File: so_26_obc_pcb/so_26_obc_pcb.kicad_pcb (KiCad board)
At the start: 4 copper layers, 90.2 x 95.9 mm, 52 parts, among them J1 Conn_02x12_Odd_Even, J10 Conn_01x02, J2 Conn_02x06_Odd_Even, J3 Conn_01x04, J4 Conn_01x03, J5 Conn_01x02, J7 Conn_01x03, J8 Conn_01x03, J9 Conn_01x02, SW1 SW_Push, U1 STM32G431RBTx, U2 TPT3232A-TS3R, U3 PCT2075, U4 MPRLS0025, U5 LSM6DS3, U6 MEM2067-02-180-00-A

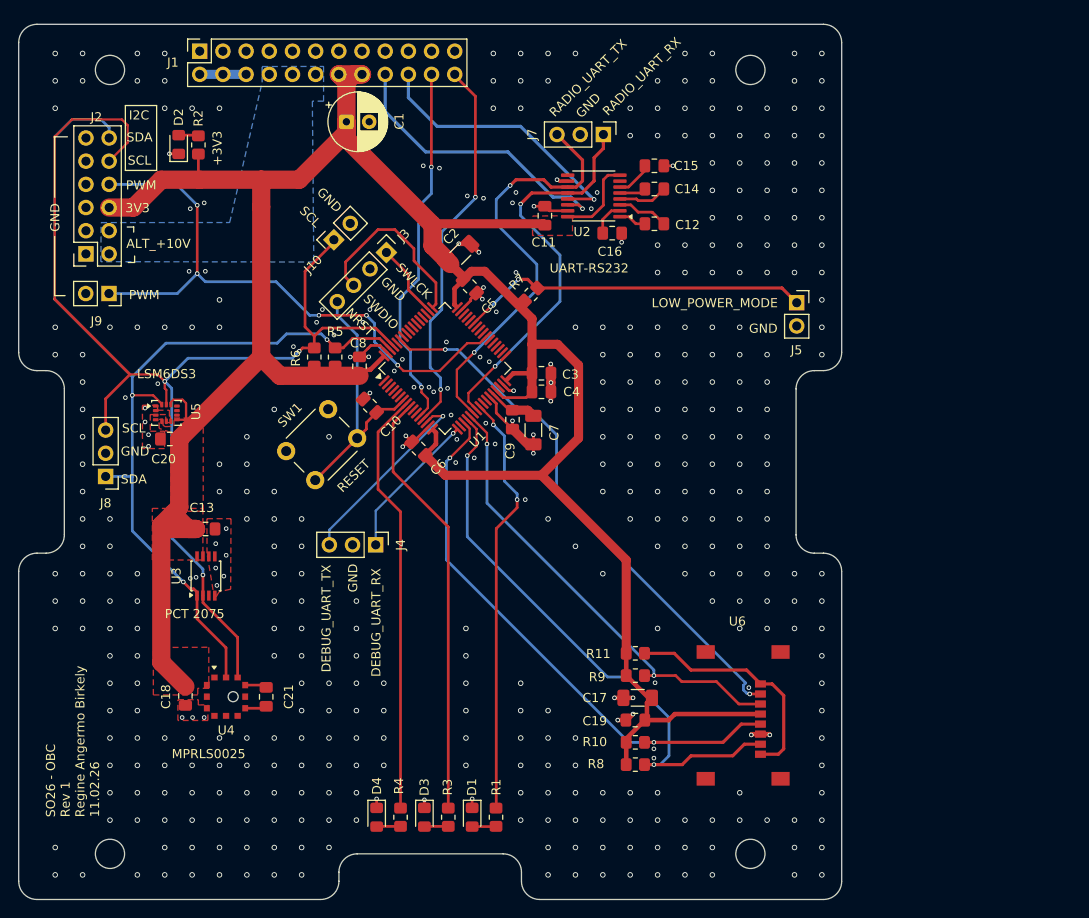
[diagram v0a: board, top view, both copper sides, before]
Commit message: PCB: Placed components and IC's
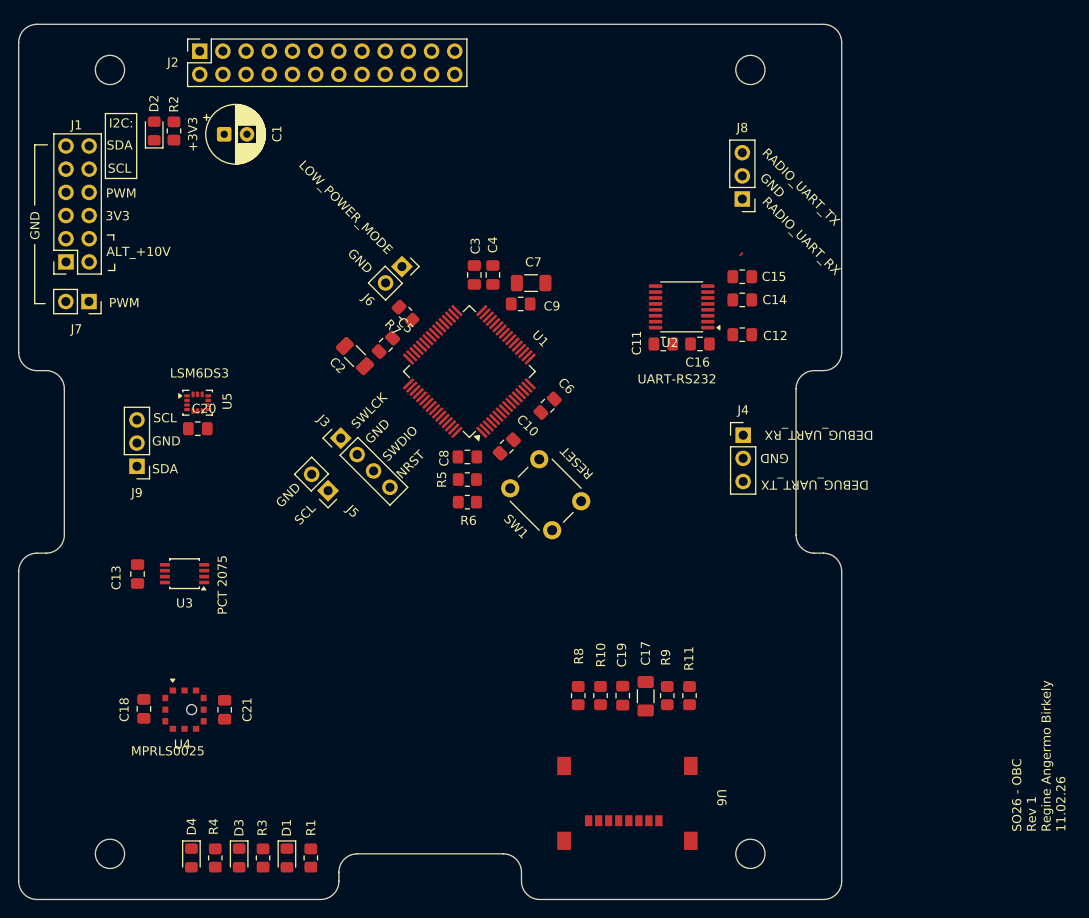
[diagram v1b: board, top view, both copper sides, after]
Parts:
- moved J6 43.4 mm to (98.0, 71.8), turned to -45 degrees
- moved J4 42.0 mm to (135.4, 90.3), turned to 0 degrees
- moved U6 28.1 mm to (122.0, 139.3), turned to 0 degrees
- moved J5 27.5 mm to (89.9, 96.4), turned to -135 degrees
- moved R6 23.1 mm to (105.2, 97.7), turned to 180 degrees
- moved J3 20.9 mm to (91.3, 90.6), turned to 45 degrees
- moved D1 20.8 mm to (85.4, 136.6)
- moved D3 20.8 mm to (80.2, 136.6)
- moved D4 20.8 mm to (74.9, 136.6)
- moved R4 20.8 mm to (77.5, 136.6)
- moved R1 20.8 mm to (88.0, 136.6)
- moved R3 20.8 mm to (82.8, 136.6)
- moved SW1 20.1 mm to (113.0, 93.0), turned to -45 degrees
- moved R5 19.7 mm to (105.2, 95.2), turned to 180 degrees
- moved C11 19.1 mm to (126.6, 80.3), turned to 0 degrees
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- renumbered J2 to J1, J1 to J2, J10 to J5, J5 to J6, J9 to J7, J7 to J8, J8 to J9
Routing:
- net +3V3: track 294.5 -> 0.00 mm
- net /BOOT0: track 134.4 -> 0.00 mm, vias 3 -> 0
- net /I2C_SDA: track 114.0 -> 0.00 mm, vias 3 -> 0
- net /PWM_HEATER: track 67.5 -> 0.00 mm, vias 5 -> 0
- net /SD_MISO: track 63.9 -> 0.00 mm, vias 2 -> 0
- net /SD_SCK: track 60.9 -> 0.00 mm, vias 2 -> 0
- net /SD_CS: track 60.2 -> 0.00 mm, vias 2 -> 0
- net GND: track 52.7 -> 0.00 mm, vias 429 -> 0
- net /SD_MOSI: track 50.7 -> 0.00 mm, vias 2 -> 0
- net /LED_YELLOW: track 47.3 -> 0.00 mm
- net /RADIO_UART_TX: track 46.8 -> 0.00 mm, vias 2 -> 0
- net /LED_GREEN: track 46.7 -> 0.00 mm
- net /LED_BLUE: track 46.6 -> 0.00 mm, vias 2 -> 0
- net /RADIO_UART_RX: track 43.5 -> 1.24 mm, vias 2 -> 0
- net /VBAT_1: track 42.1 -> 0.00 mm, vias 2 -> 0
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- removed copper zone on F.Cu, net +3V3
- removed copper zone on B.Cu, net ALT_+10V
- removed copper zone on F.Cu, net GND
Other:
- board text added: "I2C:"
- board text removed: "I2C"

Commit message: PCB: did some routing, almost done
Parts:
- removed J9: Conn_01x03, Connector_PinHeader_2.54mm:PinHeader_1x03_P2.54mm_Vertical
- added J10: Conn_01x04, Connector_PinHeader_2.54mm:PinHeader_1x04_P2.54mm_Vertical, F.Cu at (66.7, 96.0)
- moved C1 12.9 mm to (91.4, 57.0)
- moved U5 6.56 mm to (74.0, 93.1), turned to 180 degrees
- moved C13 5.86 mm to (74.0, 102.5), turned to 0 degrees
- moved C20 1.81 mm to (73.9, 90.3)
- moved U3 1.47 mm to (74.0, 107.0), turned to 90 degrees
- moved D2 1.20 mm to (70.2, 56.0)
- moved R2 1.20 mm to (72.3, 56.0)
- turned C17 to -90 degrees
- turned C19 to -90 degrees
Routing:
- net +3V3: track 0.00 -> 287.5 mm, vias 0 -> 2
- net /I2C_SDA: track 0.00 -> 127.1 mm, vias 0 -> 6
- net /BOOT0: track 0.00 -> 116.0 mm, vias 0 -> 3
- net /SD_MOSI: track 0.00 -> 68.7 mm, vias 0 -> 2
- net /LED_GREEN: track 0.00 -> 66.7 mm, vias 0 -> 2
- net /LED_YELLOW: track 0.00 -> 66.3 mm, vias 0 -> 2
- net /LED_BLUE: track 0.00 -> 66.2 mm, vias 0 -> 2
- net /SD_SCK: track 0.00 -> 65.4 mm, vias 0 -> 2
- net /SD_CS: track 0.00 -> 64.5 mm, vias 0 -> 2
- net /SD_MISO: track 0.00 -> 62.6 mm, vias 0 -> 2
- net /NRST: track 0.00 -> 47.2 mm, vias 0 -> 2
- net /RADIO_TX: track 0.04 -> 43.3 mm
- net /VBAT_0: track 0.00 -> 41.0 mm, vias 0 -> 2
- net /PWM_HEATER: track 0.00 -> 39.5 mm, vias 0 -> 1
- net /RADIO_RX: track 0.00 -> 38.9 mm
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- added copper zone on F.Cu, net +3V3
- added copper zone on B.Cu, net ALT_+10V
- added copper zone on F.Cu, net GND

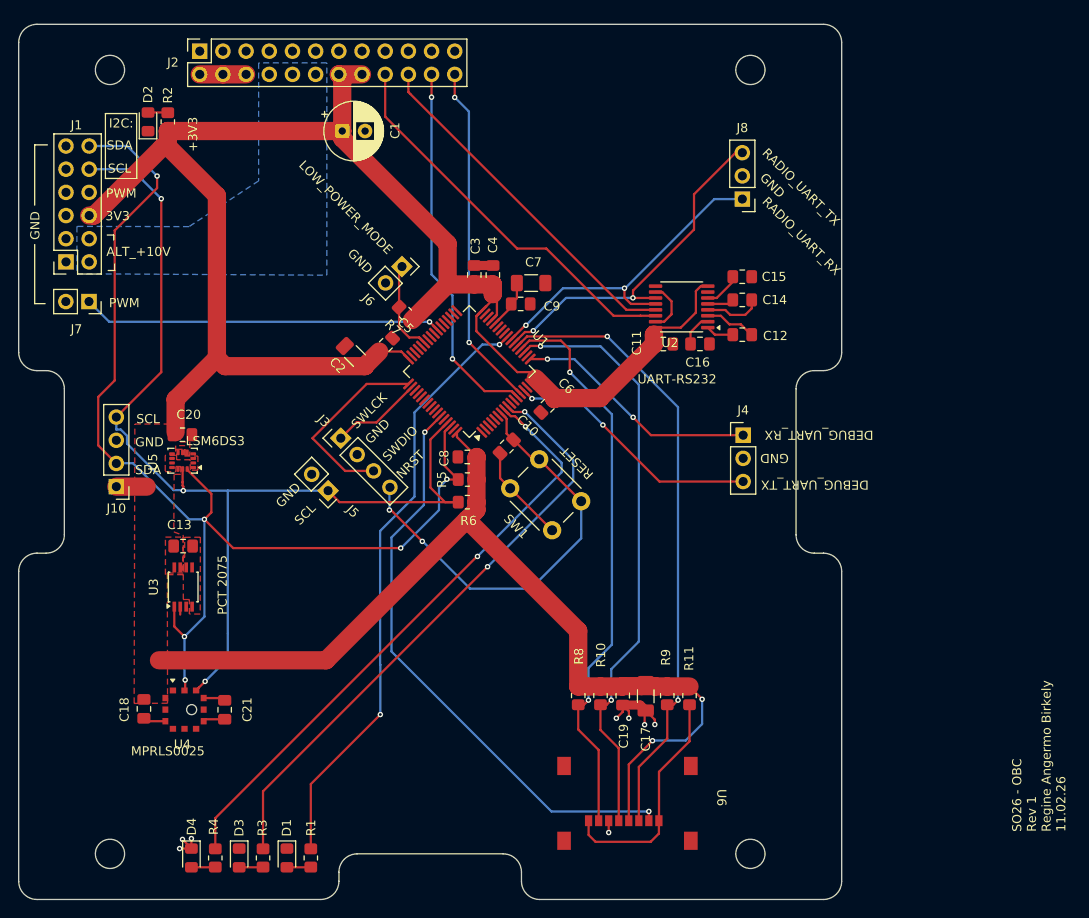
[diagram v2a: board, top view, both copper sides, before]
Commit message: PCB: Finished routing, did DRC.
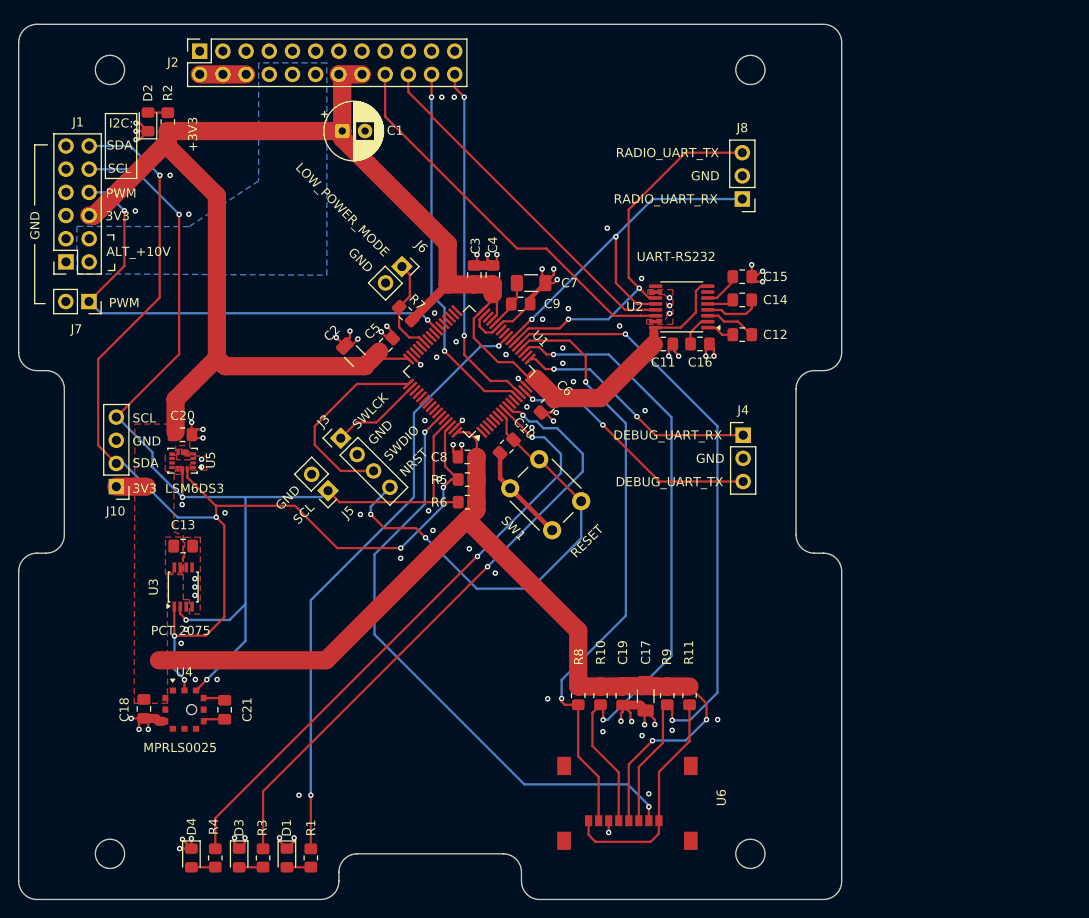
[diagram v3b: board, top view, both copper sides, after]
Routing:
- net GND: track 35.9 -> 99.3 mm, vias 8 -> 95
- net /PWM_HEATER: track 39.5 -> 55.7 mm, vias 1 -> 2
- net /SD_MOSI: track 68.7 -> 78.0 mm
- net /BOOT0: track 116.0 -> 124.7 mm, vias 3 -> 4
- net /SD_SCK: track 65.4 -> 72.2 mm
- net /RADIO_UART_RX: track 37.3 -> 43.1 mm
- net /I2C_SDA: track 127.1 -> 131.3 mm
- net /SD_MISO: track 62.6 -> 66.4 mm
- net /RADIO_UART_TX: track 38.8 -> 42.6 mm
- net /NRST: track 47.2 -> 50.4 mm
- net +3V3: track 287.5 -> 290.2 mm
- net /SD_CS: track 64.5 -> 66.4 mm
- net /LED_YELLOW: track 66.3 -> 68.2 mm
- net /VBAT_1: track 38.1 -> 39.1 mm
- net /LOW_POWER_MODE: track 10.3 -> 11.0 mm
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
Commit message: PCB: Finished rev2, I think
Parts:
- added G***: LOGO, LOGO, B.Cu at (131.5, 125.4)
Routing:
- net /SD_CS: track 66.4 -> 67.9 mm
- net /BOOT0: track 124.7 -> 125.7 mm
- net GND: vias 95 -> 692
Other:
- board text added: "I wanna be a teddy bear ...being a human is unBEARable!"
- board text added: "Regine Angermo Birkely Suborbital_CyanoSat_25/26 01.03.2026 SO26 - OBC Rev 2"
- board text removed: "SO26 - OBC Rev 1 Regine Angermo Birkely 11.02.26"

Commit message: PCB: Final review rev2
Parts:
- moved R1 2.45 mm to (87.5, 134.2)
- moved R3 2.45 mm to (82.3, 134.2)
- moved D1 2.45 mm to (84.9, 134.2)
- moved D3 2.45 mm to (79.7, 134.2)
- moved D4 2.45 mm to (74.4, 134.2)
- moved R4 2.45 mm to (77.0, 134.2)
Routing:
- net /LED_BLUE: track 66.2 -> 64.0 mm
- net /LED_YELLOW: track 68.2 -> 66.0 mm
- net /LED_GREEN: track 67.2 -> 65.0 mm
- net /VBAT_0: track 41.0 -> 42.7 mm
- net /VBAT_1: track 39.1 -> 38.6 mm
- net GND: vias 692 -> 689
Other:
- board text added: "LED_B"
- board text added: "LED_G"
- board text added: "LED_Y"
